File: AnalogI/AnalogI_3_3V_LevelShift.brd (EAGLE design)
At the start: 64 x 82 mm, 78 parts, among them IC1 HCPL-7800, IC2 HCPL-7800, IC3 HCPL-7800, IC4 HCPL-7800, IC5 MCP3424SOIC, IC6 74HC4051_MUXN, IC7 74HC4051_MUXN, P1 DF11-06-2DSA, Q1 BS170, Q2 BS170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

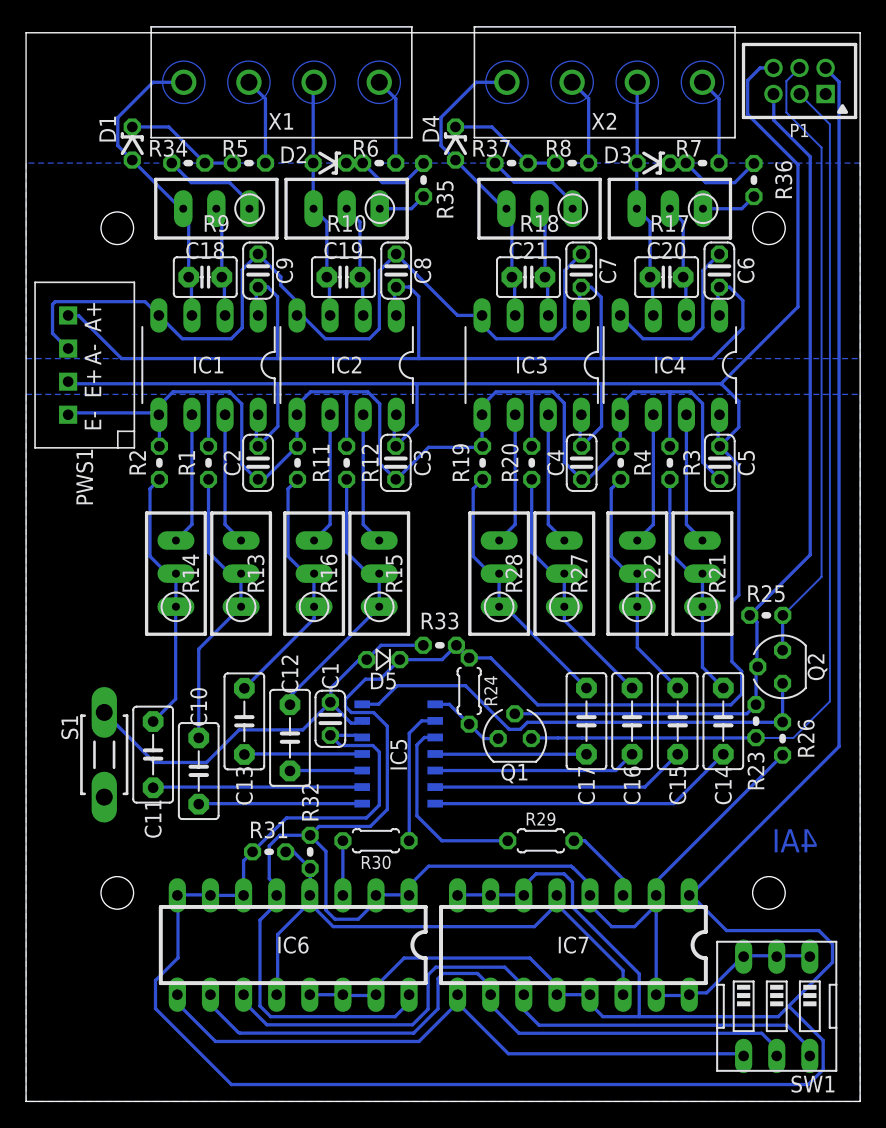
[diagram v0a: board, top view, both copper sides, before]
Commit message: Add capacitors on dc/dc isolator.
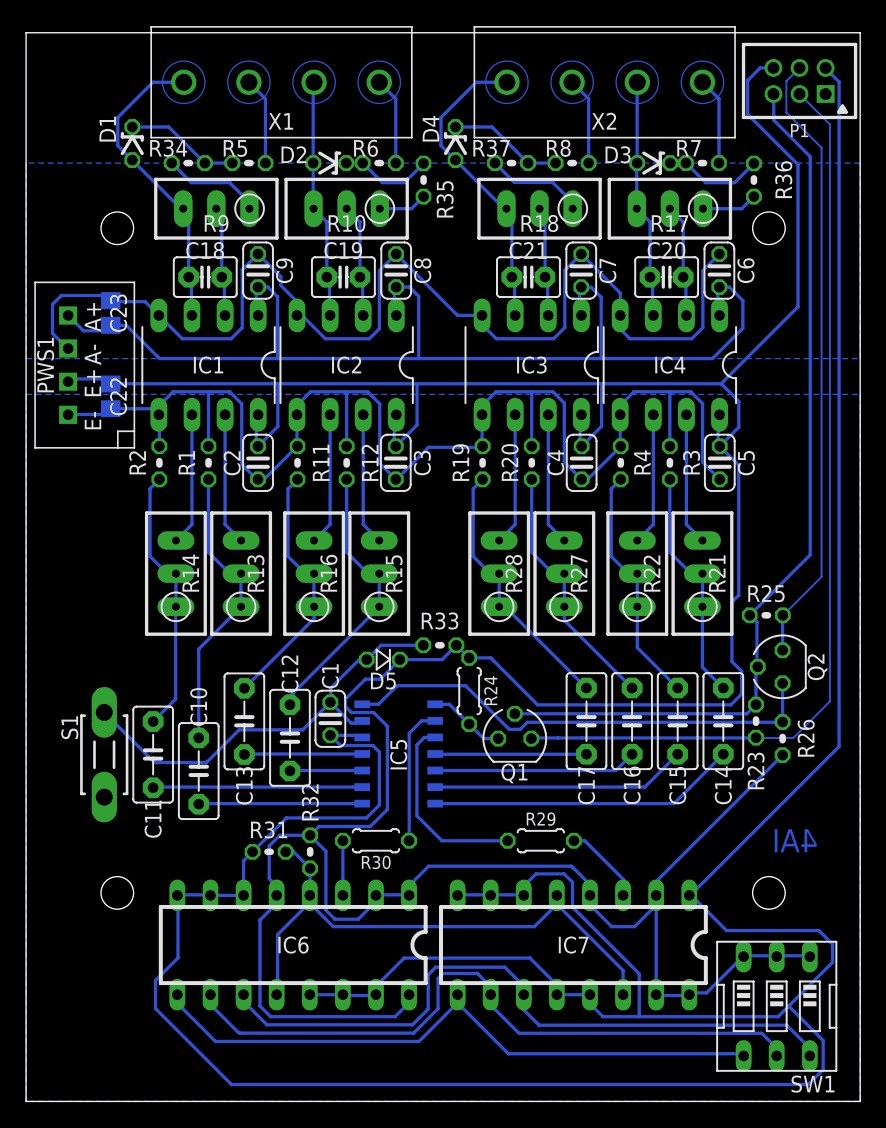
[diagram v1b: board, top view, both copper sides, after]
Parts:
- added C22: 4.7uF, rcl:C0805
- added C23: 10uF, rcl:C0805
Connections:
- net +5V: now also C22.1
- net GND: now also C22.2
- net N$33: now also C23.1
- net N$8: now also C23.2
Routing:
- net N$33: track 81.9 -> 89.1 mm
